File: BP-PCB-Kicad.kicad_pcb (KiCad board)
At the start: 2 copper layers, 98 x 120.7 mm, 21 parts, among them IC1 LMT84DCKT, J10 A3C-4DA-2DSA_71_, J12 A3C-4DA-2DSA_71_, J16 DF14-15P-1.25H52, J17 DF14-30P-1.25H_35_, J18 DF14-15P-1.25H52, J19 DF14-15P-1.25H52, J20 A3C-50DA-2DSA_71_, J21 A3C-50DA-2DSA_71_, J22 A3C-50DA-2DSA_71_, J23 A3C-50DA-2DSA_71_, J24 A3C-50DA-2DSA_71_, J25 Molex 55460-0272, J26 Molex 55460-0272, J27 Molex 55460-0272, J28 Conn_01x20, J29 Conn_01x20, J7 A3C-4DA-2DSA_71_, J9 A3C-4DA-2DSA_71_, U1 SN74CB3Q3257DBQR, U2 SN74CB3Q3257DBQR

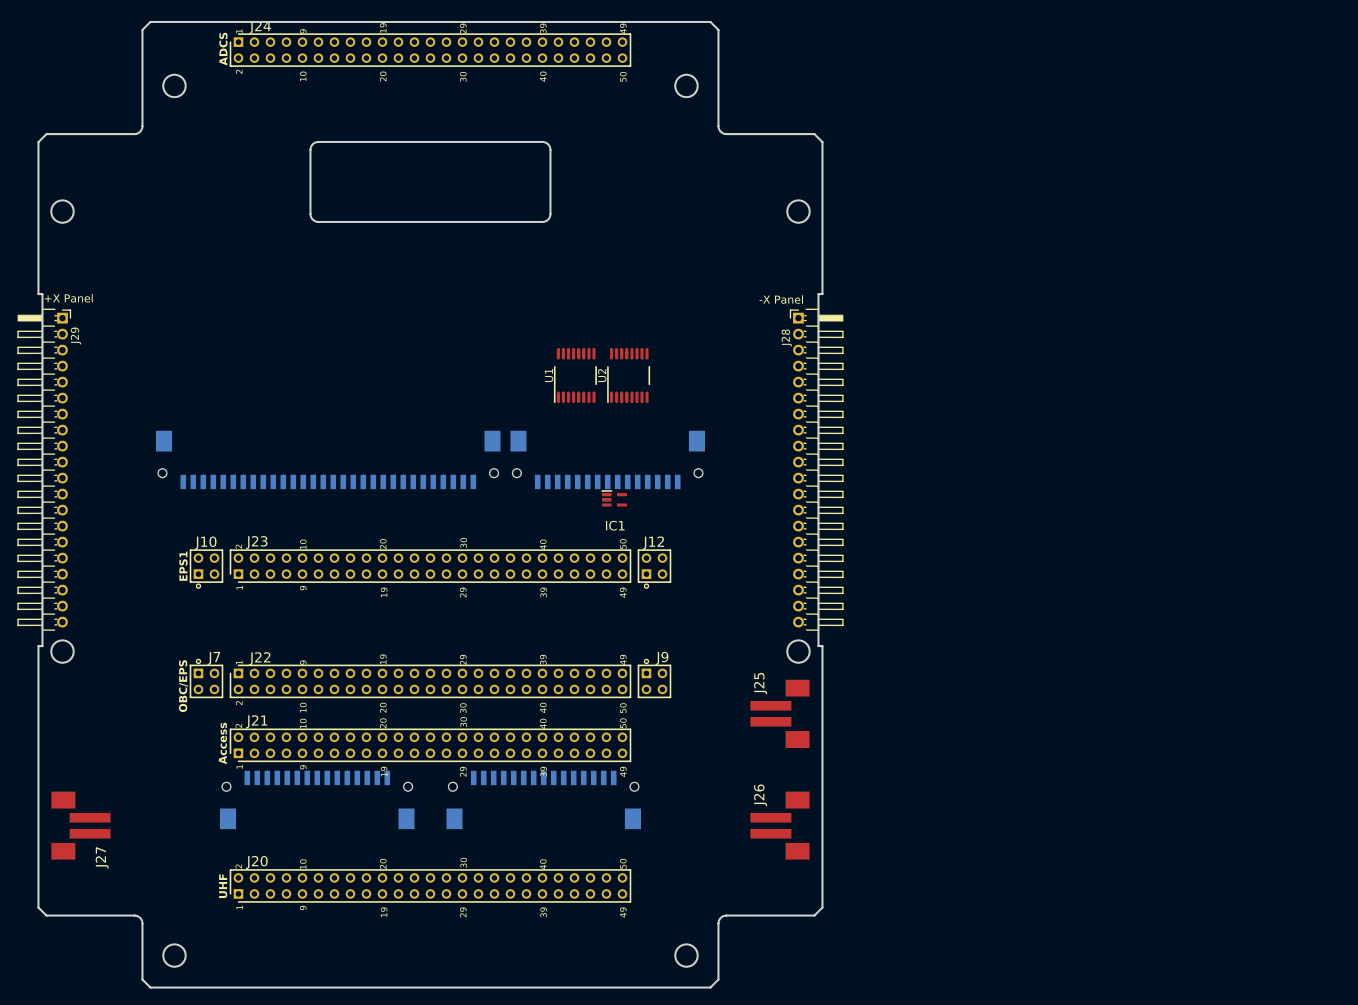
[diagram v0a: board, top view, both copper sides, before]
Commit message: Fixed errors in schematics
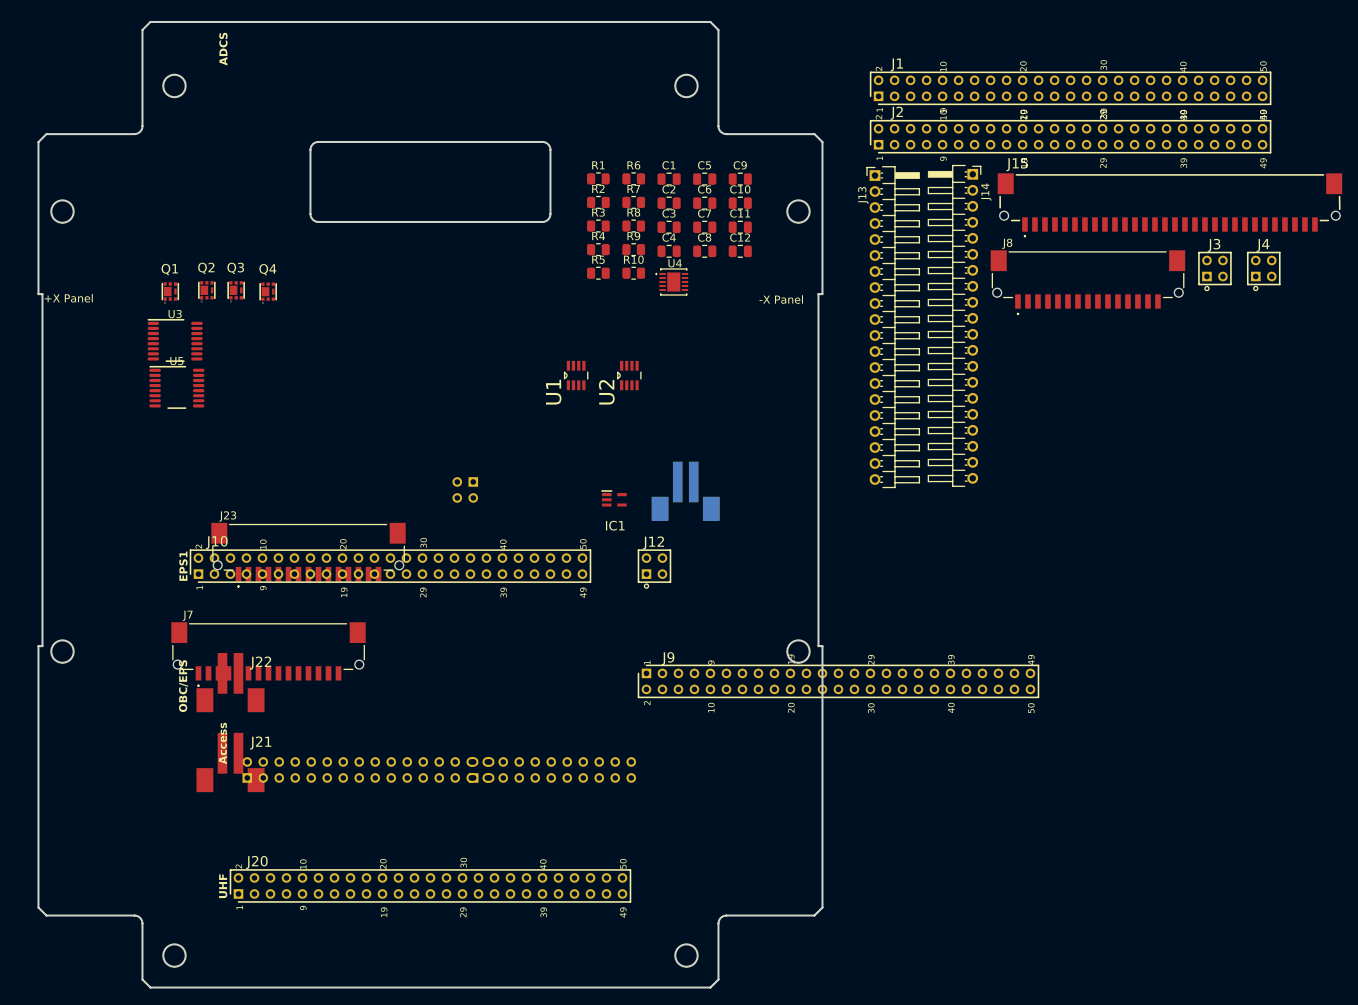
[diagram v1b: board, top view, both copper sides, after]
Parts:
- removed J24: A3C-50DA-2DSA_71_, Custom-Footprints:Hirose_A3C-50DA-2DSC(71)_Mirrored
- removed J25, J26, J27: Molex 55460-0272, Custom-Footprints:Molex_0554600272
- removed J28: Conn_01x20, Custom-Footprints:PSR-210153-20_P2.00mm
- removed J29: Conn_01x20, Custom-Footprints:PSR-210153-20_P2.00mm_Mirrored
- added C1: 1uF, Capacitor_SMD:C_0805_2012Metric, F.Cu at (98.8, 39.6)
- added C10: 47nF, Capacitor_SMD:C_0805_2012Metric, F.Cu at (107.7, 42.6)
- added C11: 0.1uF, Capacitor_SMD:C_0805_2012Metric, F.Cu at (107.7, 45.7)
- added C12: 22uF, Capacitor_SMD:C_0805_2012Metric, F.Cu at (107.7, 48.7)
- added C2: 1uF, Capacitor_SMD:C_0805_2012Metric, F.Cu at (98.8, 42.6)
- added C3: 3300pF, Capacitor_SMD:C_0805_2012Metric, F.Cu at (98.8, 45.7)
- added C4: 3300pF, Capacitor_SMD:C_0805_2012Metric, F.Cu at (98.8, 48.7)
- added C5: 4.7uF, Capacitor_SMD:C_0805_2012Metric, F.Cu at (103.3, 39.6)
- added C6: 4.7uF, Capacitor_SMD:C_0805_2012Metric, F.Cu at (103.3, 42.6)
- added C7: 0.1uF, Capacitor_SMD:C_0805_2012Metric, F.Cu at (103.3, 45.7)
- added C8: 4.7uF, Capacitor_SMD:C_0805_2012Metric, F.Cu at (103.3, 48.7)
- added C9: 220nF, Capacitor_SMD:C_0805_2012Metric, F.Cu at (107.7, 39.6)
- added J1: A3C-50DA-2DSA_71_, Custom-Footprints:Hirose_A3C-50DA-2DSC(71), F.Cu at (125.0, 29.3)
- added J13: Conn_01x20, Custom-Footprints:PSR-210153-20_P2.00mm, F.Cu at (124.6, 39.2)
- added J14: Conn_01x20, Custom-Footprints:PSR-210153-20_P2.00mm_Mirrored, F.Cu at (136.8, 39.0)
- added J15: DF14-30P-1.25H_35_, Custom-Footprints:Hirose_DF14-30P-1.25H(35), F.Cu at (143.3, 45.3)
- added J2: A3C-50DA-2DSA_71_, Custom-Footprints:Hirose_A3C-50DA-2DSC(71), F.Cu at (125.0, 35.3)
- added J3: A3C-4DA-2DSA_71_, Custom-Footprints:Hirose_A3C-4DA-2DSA(71), F.Cu at (166.1, 51.8)
- added J4: A3C-4DA-2DSA_71_, Custom-Footprints:Hirose_A3C-4DA-2DSA(71), F.Cu at (172.2, 51.8)
- added J8: DF14-15P-1.25H52, Custom-Footprints:Hirose_DF14-15P-1.25H(52), F.Cu at (142.4, 54.9)
- added Q1: SSM6K514NU,LF, Custom-Footprints:SSM6K514NULF, F.Cu at (36.5, 53.7)
- added Q2: SSM6K514NU,LF, Custom-Footprints:SSM6K514NULF, F.Cu at (41.0, 53.5)
- added Q3: SSM6K514NU,LF, Custom-Footprints:SSM6K514NULF, F.Cu at (44.7, 53.5)
- added Q4: SSM6K514NU,LF, Custom-Footprints:SSM6K514NULF, F.Cu at (48.7, 53.7)
- added R1: 1k, Resistor_SMD:R_0805_2012Metric, F.Cu at (90.0, 39.6)
- added R10: R0603EIA (1508METRIC), Resistor_SMD:R_0805_2012Metric, F.Cu at (94.4, 51.4)
- added R2: 5 Ohm, Resistor_SMD:R_0805_2012Metric, F.Cu at (90.0, 42.6)
- added R3: 5 Ohm, Resistor_SMD:R_0805_2012Metric, F.Cu at (90.0, 45.5)
- added R4: 10K, Resistor_SMD:R_0805_2012Metric, F.Cu at (90.0, 48.5)
- added R5: 150K, Resistor_SMD:R_0805_2012Metric, F.Cu at (90.0, 51.4)
- added R6: 10K, Resistor_SMD:R_0805_2012Metric, F.Cu at (94.4, 39.6)
- added R7: 33, Resistor_SMD:R_0805_2012Metric, F.Cu at (94.4, 42.6)
- added R8: 10, Resistor_SMD:R_0805_2012Metric, F.Cu at (94.4, 45.5)
- added R9: R0603EIA (1508METRIC), Resistor_SMD:R_0805_2012Metric, F.Cu at (94.4, 48.5)
- added U3: SN74CB3Q3257DBQR, Custom-Footprints:SN74CB3Q3257DBQR, F.Cu at (37.1, 59.9)
- added U4: LTC4380IDD-4-PBF, Custom-Footprints:LTC4380IDD-4#PBF, F.Cu at (99.4, 52.5)
- added U5: SN74CB3Q3257DBQR, Custom-Footprints:SN74CB3Q3257DBQR, F.Cu at (37.3, 65.8)
- J10: value A3C-4DA-2DSA_71_ -> A3C-50DA-2DSA_71_; footprint Custom-Footprints:Hirose_A3C-4DA-2DSA(71) -> Custom-Footprints:Hirose_A3C-50DA-2DSC(71)
- J12: value A3C-4DA-2DSA_71_ -> Conn_02x25_Odd_Even
- J16: value DF14-15P-1.25H52 -> A3C-50DA-2DSA_71_; footprint Custom-Footprints:Hirose_DF14-15P-1.25H(52) -> Custom-Footprints:Hirose_A3C-50DA-2DSC(71)_Mirrored
- J17: value DF14-30P-1.25H_35_ -> A3C-4DA-2DSA_71_; footprint Custom-Footprints:Hirose_DF14-30P-1.25H(35) -> Custom-Footprints:Hirose_A3C-4DA-2DSA(71)_Mirrored
- J18: value DF14-15P-1.25H52 -> A3C-4DA-2DSA_71_; footprint Custom-Footprints:Hirose_DF14-15P-1.25H(52) -> Custom-Footprints:Hirose_A3C-4DA-2DSA(71)_Mirrored
- J19: value DF14-15P-1.25H52 -> Molex 55460-0272; footprint Custom-Footprints:Hirose_DF14-15P-1.25H(52) -> Custom-Footprints:Molex_0554600272
- J20: value A3C-50DA-2DSA_71_ -> Conn_02x25_Odd_Even
- J21: value A3C-50DA-2DSA_71_ -> Molex 55460-0272; footprint Custom-Footprints:Hirose_A3C-50DA-2DSC(71) -> Custom-Footprints:Molex_0554600272
- J22: value A3C-50DA-2DSA_71_ -> Molex 55460-0272; footprint Custom-Footprints:Hirose_A3C-50DA-2DSC(71)_Mirrored -> Custom-Footprints:Molex_0554600272
- J23: value A3C-50DA-2DSA_71_ -> DF14-15P-1.25H52; footprint Custom-Footprints:Hirose_A3C-50DA-2DSC(71) -> Custom-Footprints:Hirose_DF14-15P-1.25H(52)
- J7: value A3C-4DA-2DSA_71_ -> DF14-15P-1.25H52; footprint Custom-Footprints:Hirose_A3C-4DA-2DSA(71)_Mirrored -> Custom-Footprints:Hirose_DF14-15P-1.25H(52)
- J9: value A3C-4DA-2DSA_71_ -> A3C-50DA-2DSA_71_; footprint Custom-Footprints:Hirose_A3C-4DA-2DSA(71)_Mirrored -> Custom-Footprints:Hirose_A3C-50DA-2DSC(71)_Mirrored
- U1, U2: value SN74CB3Q3257DBQR -> LTC4361CTS8-2TRMPBF; footprint Custom-Footprints:SN74CB3Q3257DBQR -> Custom-Footprints:LTC4361HTS8
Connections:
- J10 pad 1: GND_SYS -> PGC
- J10 pad 2: GND_SYS -> PGD
- J10 pad 3: SUP_UNREG_3 -> MCLR_EpsPIC
- J10 pad 4: SUP_UNREG_3 -> MCLR_ResetPIC
- J12 pad 1: SUP_12V -> (no net)
- J12 pad 2: SUP_12V -> (no net)
- J12 pad 3: RAW_POWER -> (no net)
- J12 pad 4: RAW_POWER -> (no net)
- J16 pad 1:  V_IN (Unreg2 OCP to S-band TX) -> PGC
- J16 pad 10: SBAND_TX_TEMP2 (sensor - terminal) -> OBC-ADCS_DIO_ON/OFF (MainPIC_to_ADCS)
- J16 pad 11: GND_SYS -> DIO_Thruster_ON/OFF
- J16 pad 12: unconnected-(J16-Pad12) -> MCLR_StartPIC
- J16 pad 14: unconnected-(J16-Pad14) -> GND_SYS
- J16 pad 15: OBC-SBAND_TX_UART_HK (Sband_TX_to_ComPic) -> SUP_5V_1
- J16 pad 2: SBAND_TX_TEMP1 (sensor + terminal)  -> PGD
- J16 pad 3: unconnected-(J16-Pad3) -> DIO_MUX_SEL
- J16 pad 4: OBC-SBAND_TX_UART_CONFIG (ComPIC_to_Sband_TX) -> MCLR_ResetPIC
- J16 pad 5: OBC-SBAND_TX_DATA_UART (ComPIC_to_Sband_TX) -> MCLR_ComPIC
- J16 pad 6: OBC-SBAND_TX_RTS (Sband_TX_to_ComPic) -> MCLR_MainPIC
- J16 pad 7: unconnected-(J16-Pad7) -> UART (UHF_to_ComPIC)
- J16 pad 8: GND_SYS -> UART (ComPIC_to_UHF)
- J16 pad 9: GND_SYS -> OBC-CCB_DIO_ON/OFF (MainPIC_to_CCB)
- J17 pad 1: OBC-CCB DIO ON/OFF (MainPIC_to_CCB) -> GND_SYS
- J17 pad 2: MUX-CCB_UART (MainPIC_to_CCB) -> GND_SYS
- J17 pad 3: MUX-CCB_UART (CCB_to_MainPIC) -> SUP_UNREG_3
- J17 pad 4: UART (CCB_to_ADCS) -> SUP_UNREG_3
- J18 pad 1: S-band_RX_NRZ_1K_DATA -> SUP_12V
- J18 pad 2: S-band_RX_NRZ_1K_CLK -> SUP_12V
- J18 pad 3: S-band_RX_NRZ_4K_DATA -> RAW_POWER
- J18 pad 4: unconnected-(J18-Pad4) -> RAW_POWER
- J19 pad 1: SUP_12V -> DEP_SW3
- J19 pad 2: SUP_12V -> GND_SYS
- J20 pad 1: unconnected-(J20-Pad1) -> (no net)
- J20 pad 10: unconnected-(J20-Pad10) -> (no net)
- J20 pad 11: unconnected-(J20-Pad11) -> (no net)
- J20 pad 12: unconnected-(J20-Pad12) -> (no net)
- J20 pad 13: GND_SYS -> (no net)
- J20 pad 14: GND_SYS -> (no net)
- J20 pad 15: SUP_5V_1 -> (no net)
- J20 pad 16: SUP_5V_1 -> (no net)
- J20 pad 17: unconnected-(J20-Pad17) -> (no net)
- J20 pad 18: unconnected-(J20-Pad18) -> (no net)
- J20 pad 19: unconnected-(J20-Pad19) -> (no net)
- J20 pad 2: unconnected-(J20-Pad2) -> (no net)
- J20 pad 20: unconnected-(J20-Pad20) -> (no net)
- J20 pad 21: unconnected-(J20-Pad21) -> (no net)
- J20 pad 22: unconnected-(J20-Pad22) -> (no net)
- J20 pad 23: SUP_UNREG_1 -> (no net)
- J20 pad 24: SUP_UNREG_1 -> (no net)
- J20 pad 25: SUP_5V_2 -> (no net)
- J20 pad 26: SUP_5V_2 -> (no net)
- J20 pad 27: unconnected-(J20-Pad27) -> (no net)
- J20 pad 28: unconnected-(J20-Pad28) -> (no net)
- J20 pad 29: unconnected-(J20-Pad29) -> (no net)
- J20 pad 3: unconnected-(J20-Pad3) -> (no net)
- J20 pad 30: unconnected-(J20-Pad30) -> (no net)
- J20 pad 31: unconnected-(J20-Pad31) -> (no net)
- J20 pad 32: unconnected-(J20-Pad32) -> (no net)
- J20 pad 33: unconnected-(J20-Pad33) -> (no net)
- J20 pad 34: unconnected-(J20-Pad34) -> (no net)
- J20 pad 35: SUP_UNREG_2 -> (no net)
- J20 pad 36: SUP_UNREG_2 -> (no net)
- J20 pad 37: unconnected-(J20-Pad37) -> (no net)
- J20 pad 38: unconnected-(J20-Pad38) -> (no net)
- J20 pad 39: unconnected-(J20-Pad39) -> (no net)
- J20 pad 4: unconnected-(J20-Pad4) -> (no net)
- J20 pad 40: unconnected-(J20-Pad40) -> (no net)
- J20 pad 41: unconnected-(J20-Pad41) -> (no net)
- J20 pad 42: unconnected-(J20-Pad42) -> (no net)
- J20 pad 43: unconnected-(J20-Pad43) -> (no net)
- J20 pad 44: DIO_1 (ComPIC_to_GMSK_EN) -> (no net)
- J20 pad 45: DIO_2 (ComPIC_to_CW_EN) -> (no net)
- J20 pad 46: DIO_3 (ComPIC_to_UHF CW_KEY) -> (no net)
- J20 pad 47: ANALOG_TEMP (UHF_to_RelayPIC) -> (no net)
- J20 pad 48: ANALOG_RSSI (UHF_to_RelayPIC) -> (no net)
- J20 pad 49: SUP_3V3_1 -> (no net)
- J20 pad 5: unconnected-(J20-Pad5) -> (no net)
- J20 pad 50: SUP_3V3_1 -> (no net)
- J20 pad 6: unconnected-(J20-Pad6) -> (no net)
- J20 pad 7: UART (UHF_to_ComPIC) -> (no net)
- J20 pad 8: UART (ComPIC_to_UHF) -> (no net)
- J20 pad 9: unconnected-(J20-Pad9) -> (no net)
- J21 pad 1: PGC -> DEP_SW12
- J21 pad 2: PGD -> GND_SYS
- J22 pad 1: PGC -> DEP_SW4
- J22 pad 2: PGD -> GND_SYS
- J23 pad 1: PGC -> SUP_12V
- J23 pad 10: TEMP_+Y -> DIO_Thruster_Active
- J23 pad 11: POWERSC_-Z (nc) -> DIO_Fault_Indicator
- J23 pad 12: POWERSC_-Z (nc) -> DIO_HW_Reset
- J23 pad 13: GND_SYS -> Thruster_1
- J23 pad 14: GND_SYS -> Thruster_2
- J23 pad 15: SUP_5V_1 -> Thruster_3
- J23 pad 2: PGD -> SUP_12V
- J23 pad 3: MCLR_EpsPIC -> GND_SYS
- J23 pad 4: unconnected-(J23-Pad4) -> GND_SYS
- J23 pad 5: unconnected-(J23-Pad5) -> SUP_3V3
- J23 pad 6: unconnected-(J23-Pad6) -> GND_SYS
- J23 pad 7: POWERSC_+Y -> MUX-Thruster UART_1 (MainPIC_to_Thruster)
- J23 pad 8: POWERSC_+Y -> MUX-Thruster UART_1 (Thruster_to_MainPIC)
- J23 pad 9: TEMP_-Z -> DIO_Thruster_ON/OFF
- J7 pad 1: GND_SYS ->  V_IN (Unreg2 OCP to S-band TX)
- J7 pad 2: GND_SYS -> SBAND_TX_TEMP1 (sensor + terminal) 
- J7 pad 3: SUP_UNREG_3 -> unconnected-(J7-Pad3)
- J7 pad 4: SUP_UNREG_3 -> OBC-SBAND_TX_UART_CONFIG (ComPIC_to_Sband_TX)
- J9 pad 1: SUP_12V -> PGC
- J9 pad 2: SUP_12V -> PGD
- J9 pad 3: RAW_POWER -> MUX-ADCS UART (MainPIC_to_ADCS)
- J9 pad 4: RAW_POWER -> MUX-ADCS UART (ADCS_to_MainPIC)
- U1 pad 1: DIO_MUX_SEL -> GND
- U1 pad 2: MUX-ADCS UART (MainPIC_to_ADCS) -> TEMP_3v3
- U1 pad 3: MUX-EPS1 UART (MainPIC_to_EPS1PIC) -> unconnected-(U1-GATEP-Pad3)
- U1 pad 4: OBC-MUX_UART (MainPIC_to_ADCSPIC/EPS1PIC) -> GND
- U1 pad 5: MUX-ADCS UART (ADCS_to_MainPIC) -> SUP_3V3_1
- U1 pad 6: MUX-EPS1 UART (EPS1PIC_to_MainPIC) -> Net-(Q1-D_1)
- U1 pad 7: OBC-MUX_UART (ADCSPIC/EPS1PIC_to_MainPIC) -> Net-(Q1-G)
- U1 pad 8: GND -> unconnected-(U1-~{PWRGD}-Pad8)
- U2 pad 1: DIO_MUX_SEL -> GND
- U2 pad 2: MUX-ADB UART_1 (MainPIC_to_RelayPIC) -> TEMP_3v3
- U2 pad 3: MUX-Thruster UART_1 (MainPIC_to_Thruster) -> unconnected-(U2-GATEP-Pad3)
- U2 pad 4: OBC-MUX UART_1 (MainPIC_to_RelayPIC/Thruster) -> GND
- U2 pad 5: MUX-Thruster UART_1 (Thruster_to_MainPIC) -> SUP_3V3_1
- U2 pad 6: MUX-ADB UART_1 (RelayPIC_to_MainPIC) -> Net-(Q2-D_1)
- U2 pad 7: OBC-MUX UART_1 (RelayPIC/Thruster_to_MainPIC) -> Net-(Q2-G)
- U2 pad 8: GND -> unconnected-(U2-~{PWRGD}-Pad8)

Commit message: Synchronized with pin mapping table and added circuits
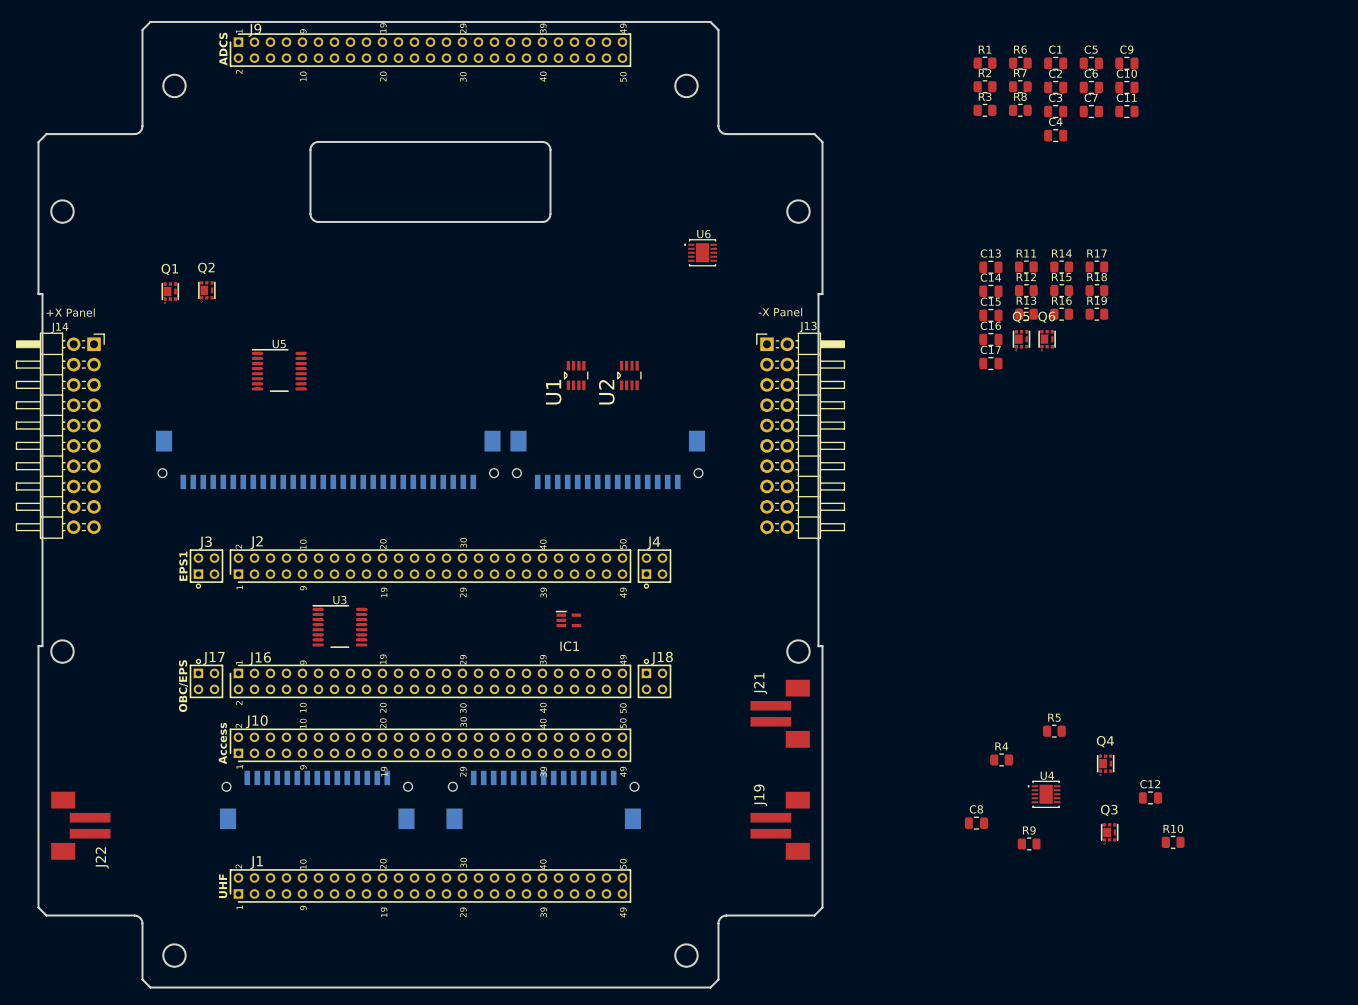
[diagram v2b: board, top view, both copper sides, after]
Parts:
- removed J12: Conn_02x25_Odd_Even, Custom-Footprints:Hirose_A3C-4DA-2DSA(71)
- removed J20: Conn_02x25_Odd_Even, Custom-Footprints:Hirose_A3C-50DA-2DSC(71)
- added C13: 4.7uF, Capacitor_SMD:C_0805_2012Metric, F.Cu at (139.1, 50.7)
- added C14: 220nF, Capacitor_SMD:C_0805_2012Metric, F.Cu at (139.1, 53.7)
- added C15: 47nF, Capacitor_SMD:C_0805_2012Metric, F.Cu at (139.1, 56.7)
- added C16: 22uF, Capacitor_SMD:C_0805_2012Metric, F.Cu at (139.1, 59.7)
- added C17: 100nF, Capacitor_SMD:C_0805_2012Metric, F.Cu at (139.1, 62.7)
- added Q5: SSM6K514NU,LF, Custom-Footprints:SSM6K514NULF, F.Cu at (142.9, 59.7)
- added Q6: SSM6K514NU,LF, Custom-Footprints:SSM6K514NULF, F.Cu at (146.1, 59.7)
- added R11: 10K, Resistor_SMD:R_0805_2012Metric, F.Cu at (143.5, 50.6)
- added R12: 150K, Resistor_SMD:R_0805_2012Metric, F.Cu at (143.5, 53.6)
- added R13: 10K, Resistor_SMD:R_0805_2012Metric, F.Cu at (143.5, 56.5)
- added R14: 33, Resistor_SMD:R_0805_2012Metric, F.Cu at (147.9, 50.6)
- added R15: 10, Resistor_SMD:R_0805_2012Metric, F.Cu at (147.9, 53.6)
- added R16: R0603EIA (1508METRIC), Resistor_SMD:R_0805_2012Metric, F.Cu at (147.9, 56.5)
- added R17: R0603EIA (1508METRIC), Resistor_SMD:R_0805_2012Metric, F.Cu at (152.3, 50.6)
- added R18: 1k, Resistor_SMD:R_0805_2012Metric, F.Cu at (152.3, 53.6)
- added R19: 1k, Resistor_SMD:R_0805_2012Metric, F.Cu at (152.3, 56.5)
- added U6: LTC4380IDD-4-PBF, Custom-Footprints:LTC4380IDD-4#PBF, F.Cu at (103.0, 48.9)
- J13: footprint Custom-Footprints:PSR-210153-20_P2.00mm -> Custom-Footprints:PSR-420253-10
- J14: footprint Custom-Footprints:PSR-210153-20_P2.00mm_Mirrored -> Custom-Footprints:PSR-420253-10_Mirrored
- J15, J23, J7, J8: moved to B.Cu
- J16, J17, J18, J19: moved to F.Cu
- R3: value 5 Ohm -> 1.67 Ohm
- moved J3 131.4 mm to (40.0, 89.0)
- moved Q3 128.5 mm to (153.9, 121.3)
- moved J1 127.8 mm to (45.0, 129.0)
- moved Q4 120.2 mm to (153.4, 112.7)
- moved J14 111.9 mm to (26.9, 60.3)
- moved R10 98.0 mm to (161.8, 122.5)
- moved J2 96.4 mm to (45.0, 89.0)
- moved J9 94.0 mm to (45.0, 22.5)
- moved J8 90.4 mm to (74.4, 114.5)
- moved R9 89.2 mm to (143.8, 122.8)
- moved C12 85.4 mm to (159.0, 117.0)
- moved J4 84.8 mm to (96.0, 89.0)
- moved R4 81.3 mm to (140.4, 112.2)
- moved R5 80.8 mm to (147.0, 108.7)
- moved U4 79.2 mm to (145.9, 116.5)
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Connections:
- net OBC-SBAND_TX_ON/OFF renamed DIO_S-Band_TX_ON/OFF
- C5 pad 1: TEMP_3v3 -> TEMP_3v3_MX
- C6 pad 1: TEMP_3v3 -> TEMP_3v3_PX
- J13 pad 3: TEMP_3v3 -> TEMP_3v3_MX
- J14 pad 3: TEMP_3v3 -> TEMP_3v3_PX
- J16 pad 38: DIO S-band RX ON/OFF -> DIO_S-Band_RX_ON/OFF
- J7 pad 10: SBAND_TX_TEMP2 (sensor - terminal) -> S-band_TX_Analog_Temperature
- Q1 pad 4: TEMP_3v3 -> TEMP_3v3_MX
- Q1 pad 7: TEMP_3v3 -> TEMP_3v3_MX
- Q2 pad 4: TEMP_3v3 -> TEMP_3v3_PX
- Q2 pad 7: TEMP_3v3 -> TEMP_3v3_PX
- U1 pad 2: TEMP_3v3 -> TEMP_3v3_MX
- U2 pad 2: TEMP_3v3 -> TEMP_3v3_PX
